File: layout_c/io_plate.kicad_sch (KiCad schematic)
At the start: 19 parts, among them J2 USB_C_Sensors, J8 Conn_01x11, J9 USB_C_Radar, U2 USBLC6-2SC6, U4 USBLC6-2SC6

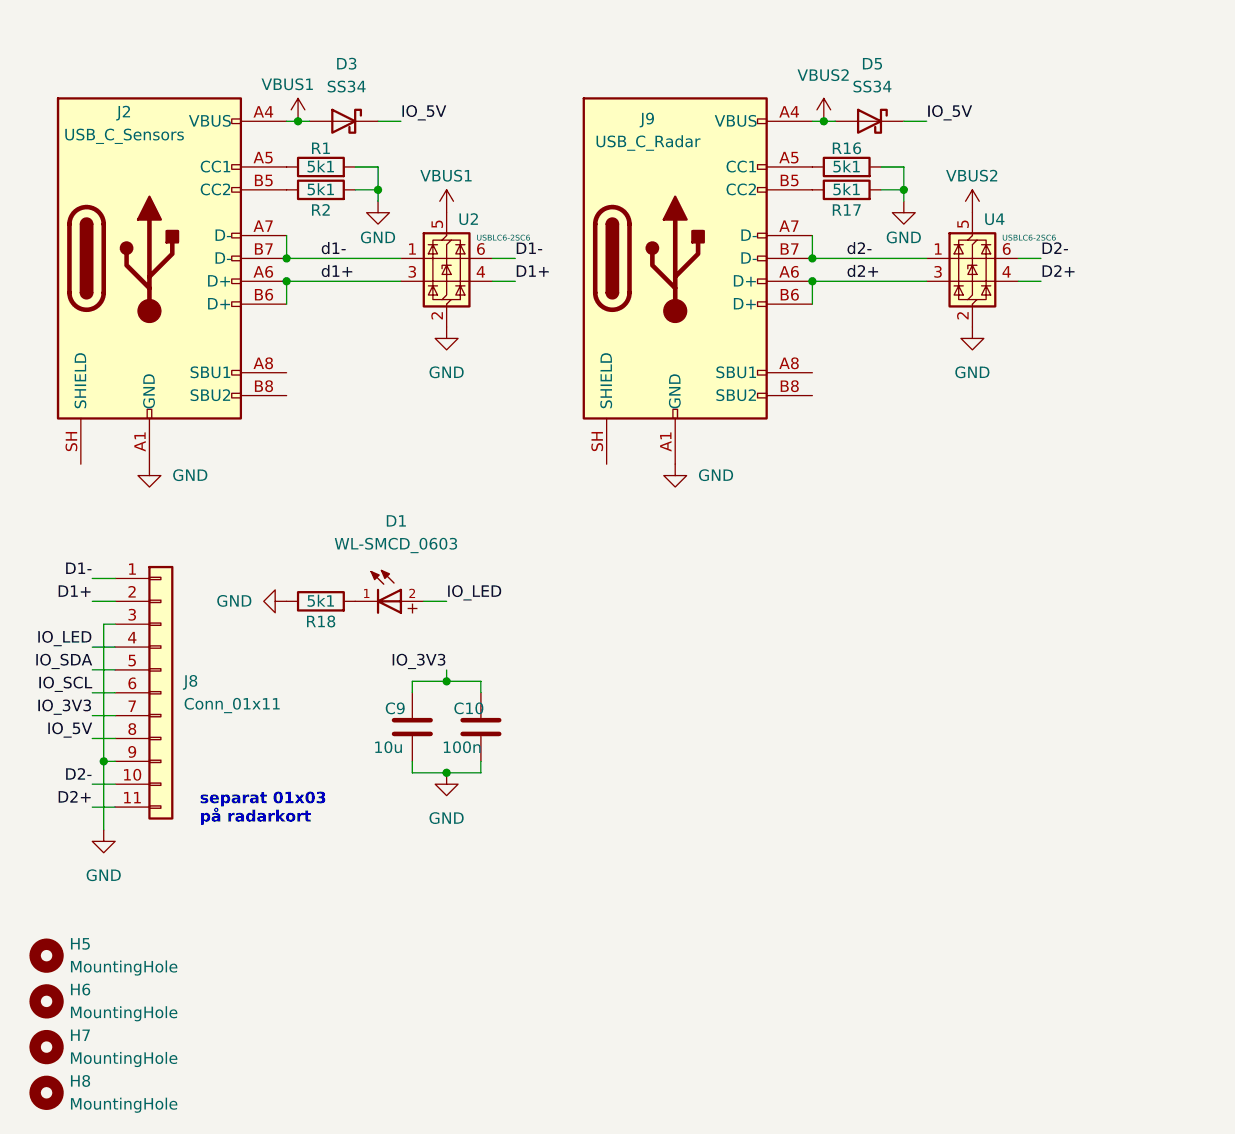
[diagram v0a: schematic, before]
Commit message: Updated usb footprints on layout C
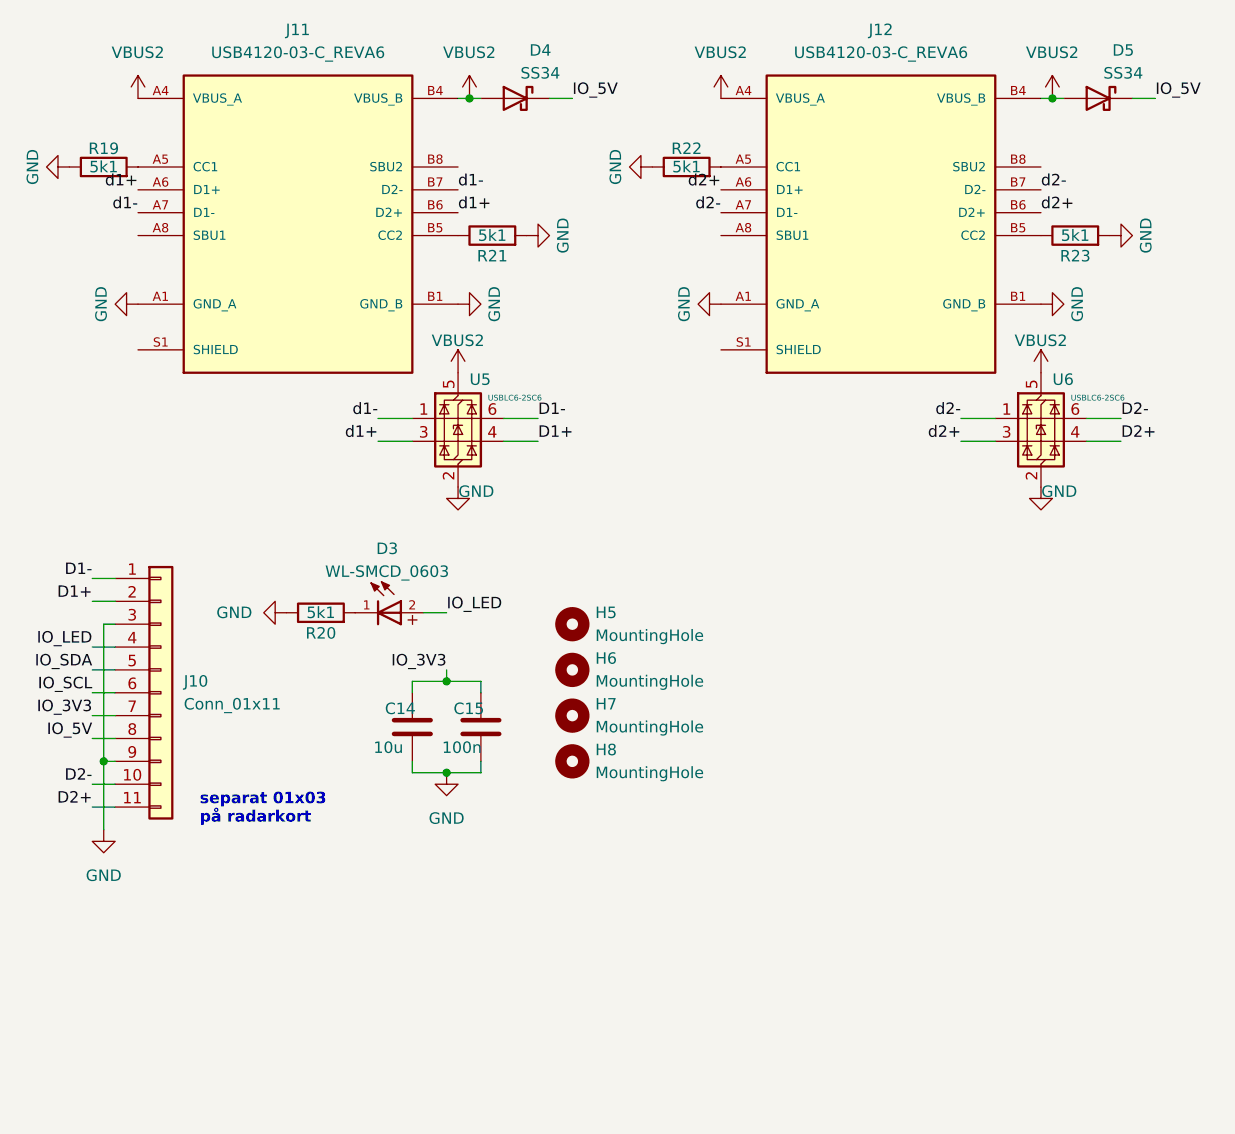
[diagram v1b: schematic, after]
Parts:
- removed D3: SS34, Diode_SMD:D_SMA, symbol Diode:SS34
- removed J2: USB_C_Sensors, Connector_USB:USB_C_Receptacle_G-Switch_GT-USB-7051x, symbol Connector:USB_C_Receptacle_USB2.0_16P
- removed J9: USB_C_Radar, Connector_USB:USB_C_Receptacle_G-Switch_GT-USB-7051x, symbol Connector:USB_C_Receptacle_USB2.0_16P
- removed R1, R16, R17, R2: 5k1, Resistor_SMD:R_0805_2012Metric, symbol Device:R
- removed U2: USBLC6-2SC6, Package_TO_SOT_SMD:SOT-23-6, symbol Power_Protection:USBLC6-2SC6
- added D4: SS34, Diode_SMD:D_SMA, symbol Diode:SS34
- added J11, J12: USB4120-03-C_REVA6, Library:GCT_USB4120-03-C_REVA6, symbol Library:USB4120-03-C_REVA6
- added R19, R21, R22, R23: 5k1, Resistor_SMD:R_0805_2012Metric, symbol Device:R
- added U5: USBLC6-2SC6, Package_TO_SOT_SMD:SOT-23-6, symbol Power_Protection:USBLC6-2SC6
- renumbered C9 to C14, C10 to C15, D1 to D3, J8 to J10, R18 to R20, U4 to U6
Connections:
- net D1+: now also U5.4 (I/O2)
- net D1-: now also U5.6 (I/O1)
- net GND: now also J11.A1 (GND_A), J11.A12 (GND_A), J11.B1 (GND_B), J11.B12 (GND_B), J12.A1 (GND_A), J12.A12 (GND_A), J12.B1 (GND_B), J12.B12 (GND_B), R19.1, R21.2, R22.1, R23.2, U5.2 (GND)
- net IO_5V: now also D4.1 (K)
- net VBUS2: now also D4.2 (A), J11.A4 (VBUS_A), J11.A9 (VBUS_A), J11.B4 (VBUS_B), J11.B9 (VBUS_B), J12.A4 (VBUS_A), J12.A9 (VBUS_A), J12.B4 (VBUS_B), J12.B9 (VBUS_B), U5.5 (VBUS)
- net d1+: now also J11.A6 (D1+), J11.B6 (D2+), U5.3 (I/O2)
- net d1-: now also J11.A7 (D1-), J11.B7 (D2-), U5.1 (I/O1)
- net d2+: now also J12.A6 (D1+), J12.B6 (D2+)
- net d2-: now also J12.A7 (D1-), J12.B7 (D2-)
- new net: J12.A5 (CC1), R22.2
- new net: J12.B5 (CC2), R23.1
- new net: J12.S1 (SHIELD), J12.S2 (SHIELD), J12.S3 (SHIELD), J12.S4 (SHIELD)
- new net: J11.A5 (CC1), R19.2
- new net: J11.B5 (CC2), R21.1
- new net: J11.S1 (SHIELD), J11.S2 (SHIELD), J11.S3 (SHIELD), J11.S4 (SHIELD)
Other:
- moved on the sheet: D3, H5, H6, H7, H8, R20, U6

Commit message: Layout C adjusted
switched to 4 layer stack
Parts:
- J10: footprint Connector_JST:JST_EH_B11B-EH-A_1x11_P2.50mm_Vertical -> Connector_JST:JST_XH_B11B-XH-A_1x11_P2.50mm_Vertical
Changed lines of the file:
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@@
 			)
 		)
-		(property "Footprint" "Connector_JST:JST_EH_B11B-EH-A_1x11_P2.50mm_Vertical"
+		(property "Footprint" "Connector_JST:JST_XH_B11B-XH-A_1x11_P2.50mm_Vertical"
 			(at 30.48 88.9 0)
 			(hide yes)

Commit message: Design improvements
started implementation of usb-c breakout board
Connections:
- net D1+: now also U5.3 (I/O2); no longer U5.4 (I/O2)
- net D1-: now also U5.1 (I/O1); no longer U5.6 (I/O1)
- net D2+: now also U6.3 (I/O2); no longer U6.4 (I/O2)
- net D2-: now also U6.1 (I/O1); no longer U6.6 (I/O1)
- net d1+: now also U5.4 (I/O2); no longer U5.3 (I/O2)
- net d1-: now also U5.6 (I/O1); no longer U5.1 (I/O1)
- net d2+: now also U6.4 (I/O2); no longer U6.3 (I/O2)
- net d2-: now also U6.6 (I/O1); no longer U6.1 (I/O1)
- net VBUS2 renamed VBUS1
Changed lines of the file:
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@@
 		)
 	)
-	(label "d2+"
+	(label "D2+"
 		(at 119.38 60.96 180)
 		(effects
@@
 		)
 	)
-	(label "D2-"
+	(label "d2-"
 		(at 137.16 58.42 0)
 		(effects
@@
 		)
 	)
-	(label "d2-"
+	(label "D2-"
 		(at 119.38 58.42 180)
 		(effects
@@
 		)
 	)
-	(label "D1+"
+	(label "d1+"
 		(at 72.39 60.96 0)
 		(effects
@@
 		)
 	)
-	(label "D1-"
+	(label "d1-"
 		(at 72.39 58.42 0)
 		(effects
@@
 		)
 	)
-	(label "d1+"
+	(label "D1+"
 		(at 54.61 60.96 180)
 		(effects
@@
 		)
 	)
-	(label "d1-"
+	(label "D1-"
 		(at 54.61 58.42 180)
 		(effects
@@
 		)
 	)
-	(label "D2+"
+	(label "d2+"
 		(at 137.16 60.96 0)
 		(effects
@@
 			)
 		)
-		(property "Value" "VBUS2"
+		(property "Value" "VBUS1"
 			(at 27.94 17.78 0)
 			(show_name no)
@@
 			)
 		)
-		(property "Value" "VBUS2"
+		(property "Value" "VBUS1"
 			(at 64.77 17.78 0)
 			(show_name no)
@@
 			)
 		)
-		(property "Value" "VBUS2"
+		(property "Value" "VBUS1"
 			(at 63.5 49.784 0)
 			(show_name no)
